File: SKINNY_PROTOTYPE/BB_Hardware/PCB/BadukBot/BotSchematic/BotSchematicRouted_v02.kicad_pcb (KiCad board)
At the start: 4 copper layers, 93 x 44.5 mm, 82 parts, among them J1 MOLEX_78171-0002, J10 A3-16DA-2SV(71), J11 62401621722, J12 A3-16DA-2SV(71), J13 0877601616, J2 MOLEX_78171-0003, M1 Pos-1a, M2 Neg-1a, M3 Pos-2a, M4 Neg-2a, P1 SWD Pads, P4 Conn_01x02_Female, P5 Pads, Q1 MMBT3904LT1G, Q2 MMBT3904LT1G, Q3 MMBT3904LT1G, Q4 MMBT3904LT1G, U1 STM32F051C8U6, U2 LSM6DS3, U3 A3901SEJTR-T, U4 ADP122ACPZ-3.3-R7, U5 AT42QT1070-MMHCT-ND, U6 MCP73831T-2ACI_OT, U7 NRF24L01P-R7, Y1 7V-16.000MAAE-T

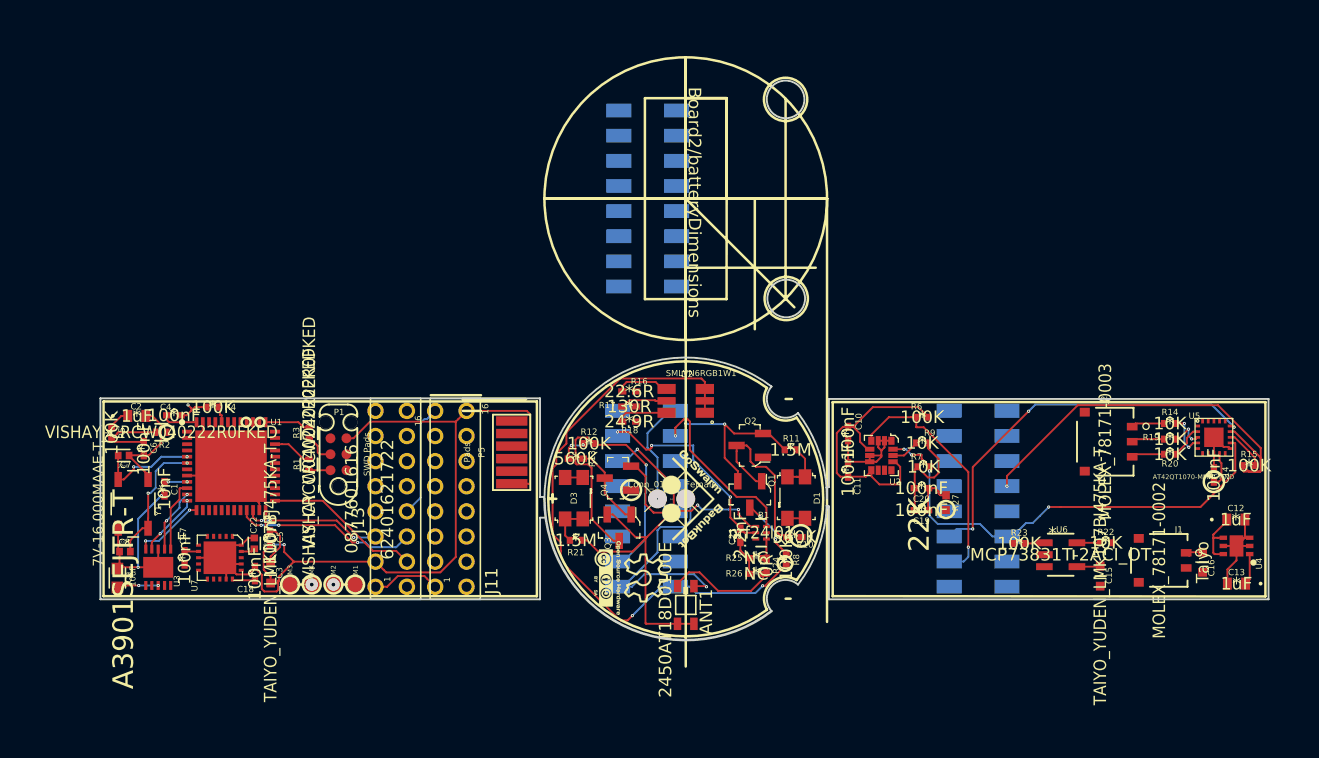
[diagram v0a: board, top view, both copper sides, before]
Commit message: Routed PCBs pending optimization
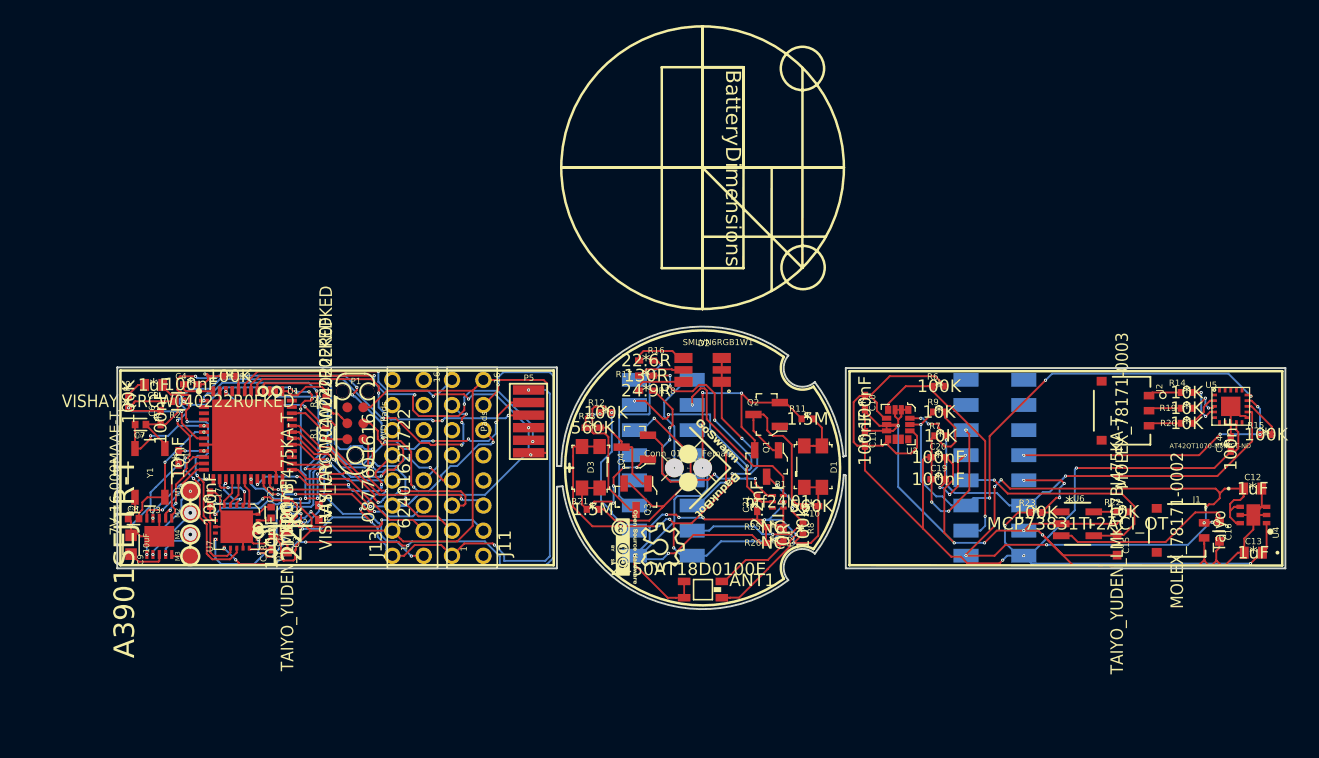
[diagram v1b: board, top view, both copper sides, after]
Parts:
- removed the J12 at (112.5, 86.3)
- J10, J12: footprint A13:A13 -> A13:A13_1
- moved R27 49.9 mm to (85.7, 111.3)
- moved M1 15.1 mm to (75.5, 109.6), turned to 180 degrees
- moved M2 12.7 mm to (75.5, 111.3), turned to 180 degrees
- moved M4 10.5 mm to (75.5, 113.1), turned to 180 degrees
- moved M3 8.26 mm to (75.5, 114.8), turned to 180 degrees
- moved C17 5.10 mm to (77.1, 110.2), turned to 270 degrees
- moved C9 2.86 mm to (70.8, 113.9)
- moved C12 2.81 mm to (160.1, 109.4)
- moved C13 2.81 mm to (160.1, 114.5)
- moved C15 2.81 mm to (149.3, 113.9)
- moved C16 2.81 mm to (157.4, 112.8)
- moved C2 2.81 mm to (72.6, 101.2)
- moved C21 2.81 mm to (120.6, 110.7)
- moved C22 2.81 mm to (81.9, 111.3)
- moved C5 2.81 mm to (83.2, 110.9)
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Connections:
- ANT1 pad 2: 2a_GND -> 23a_Ground
- ANT1 pad 3: 2a_GND -> 23a_Ground
- ANT1 pad 4: 2a_GND -> 23a_Ground
- B1 pad 2: 2a_GND -> 23a_Ground
- C1 pad 2: 2b_GND -> 23a_Ground
- C10 pad 2: 21a_3.3v -> 23a_Ground
- C11 pad 2: 21a_3.3v -> 23a_Ground
- C12 pad 2: 21a_3.3v -> 23a_Ground
- C13 pad 2: 21a_3.3v -> 23a_Ground
- C14 pad 2: 21a_3.3v -> 23a_Ground
- C15 pad 2: 21a_3.3v -> 23a_Ground
- C16 pad 2: 21a_3.3v -> 23a_Ground
- C17 pad 1: 2b_GND -> 23a_Ground
- C18 pad 1: 2b_GND -> 23a_Ground
- C19 pad 1: 2b_GND -> 23a_Ground
- C19 pad 2: 1b_3.3v -> 21a_3.3v
- C2 pad 2: 2b_GND -> 23a_Ground
- C20 pad 1: 2b_GND -> 23a_Ground
- C20 pad 2: 1b_3.3v -> 21a_3.3v
- C21 pad 2: 2a_GND -> 23a_Ground
- C22 pad 2: 2b_GND -> 23a_Ground
- C3 pad 2: 2b_GND -> 23a_Ground
- C4 pad 2: 2b_GND -> 23a_Ground
- C5 pad 2: 2b_GND -> 23a_Ground
- C6 pad 2: 2b_GND -> 23a_Ground
- C7 pad 2: 2b_GND -> 23a_Ground
- C8 pad 2: 2b_GND -> 23a_Ground
- C9 pad 2: 2b_GND -> 23a_Ground
- J1 pad 2: 21a_3.3v -> 23a_Ground
- J10 pad 2: 2a_GND -> 23a_Ground
- J11 pad 16: 2b_GND -> 23a_Ground
- J12 pad 2: 21a_3.3v -> 22a_VBAT
- J12 pad 3: 22a_VBAT -> 23a_Ground
- J13 pad 3: 2b_GND -> 23a_Ground
- P1 pad 5: 2b_GND -> 23a_Ground
- P4 pad 2: 2a_GND -> 23a_Ground
- P5 pad 6: 2b_GND -> 23a_Ground
- Q1 pad 2: 2a_GND -> 23a_Ground
- Q2 pad 2: 2a_GND -> 23a_Ground
- Q3 pad 2: 2a_GND -> 23a_Ground
- Q4 pad 2: 2a_GND -> 23a_Ground
- R11 pad 2: 2a_GND -> 23a_Ground
- R16 pad 1: Net-(R16-Pad1) -> 6a_RGBLED2
- R17 pad 1: Net-(R17-Pad1) -> 5a_RGBLED1
- R18 pad 1: Net-(R18-Pad1) -> 7a_RGBLED3
- R21 pad 1: 2a_GND -> 23a_Ground
- R22 pad 1: 21a_3.3v -> 23a_Ground
- R25 pad 2: 2a_GND -> 23a_Ground
- R26 pad 2: 2a_GND -> 23a_Ground
- R27 pad 1: 2b_GND -> 23a_Ground
- R4 pad 2: 2b_GND -> 23a_Ground
- U1 pad 23: 2b_GND -> 23a_Ground
- U1 pad 47: 2b_GND -> 23a_Ground
- U1 pad 49: 2b_GND -> 23a_Ground
- U1 pad 7: NSRT -> NRST
- U1 pad 8: 2b_GND -> 23a_Ground
- U2 pad 1: 21a_3.3v -> 23a_Ground
- U2 pad 2: 21a_3.3v -> 23a_Ground
- U2 pad 3: 21a_3.3v -> 23a_Ground
- U2 pad 6: 21a_3.3v -> 23a_Ground
- U2 pad 7: 21a_3.3v -> 23a_Ground
- U2 pad 9: 21a_3.3v -> Net-(U2-Pad9)
- U3 pad 11: 2b_GND -> 23a_Ground
- U3 pad 3: 2b_GND -> 23a_Ground
- U4 pad 2: 21a_3.3v -> 23a_Ground
- U4 pad 3: 21a_3.3v -> 23a_Ground
- U4 pad 5: 21a_3.3v -> 23a_Ground
- U4 pad 7: 21a_3.3v -> 23a_Ground
- U5 pad 11: 21a_3.3v -> 23a_Ground
- U5 pad 13: 21a_3.3v -> 23a_Ground
- U5 pad 44: 21a_3.3v -> 23a_Ground
- U5 pad 8: 21a_3.3v -> 23a_Ground
- U5 pad 9: 21a_3.3v -> 23a_Ground
- U6 pad 2: 21a_3.3v -> 23a_Ground
- U7 pad 14: 2b_GND -> 23a_Ground
- U7 pad 17: 2b_GND -> 23a_Ground
- U7 pad 20: 2b_GND -> 23a_Ground
- U7 pad 21: 2b_GND -> 23a_Ground
- U7 pad 8: 2b_GND -> 23a_Ground
- Y1 pad 2: 2b_GND -> 23a_Ground
- Y1 pad 4: 2b_GND -> 23a_Ground
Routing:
- net 23a_Ground: track 0.00 -> 212.1 mm, vias 0 -> 17
- net 2b_GND: track 111.4 -> 0.00 mm, vias 5 -> 0
- net 2a_GND: track 2.87 -> 98.3 mm, vias 1 -> 12
- net 15a_GND2: track 70.6 -> 0.00 mm, vias 4 -> 0
- net 21a_3.3v: track 53.6 -> 121.3 mm, vias 0 -> 8
- net 22a_VBAT: track 6.42 -> 72.4 mm, vias 0 -> 7
- net 12b_ANT1: track 0.00 -> 55.7 mm, vias 0 -> 8
- net 14b_VDD_PA: track 0.00 -> 51.1 mm, vias 0 -> 6
- net 13b_ANT2: track 0.00 -> 48.1 mm, vias 0 -> 7
- net 10b_SDA: track 11.0 -> 53.7 mm, vias 3 -> 7
- net 1b_3.3v: track 31.8 -> 74.4 mm, vias 4 -> 11
- net Net-(P1-Pad3): track 0.00 -> 36.1 mm, vias 0 -> 10
- net 22b_VBAT: track 0.00 -> 30.7 mm, vias 0 -> 6
- net 8b_IO1: track 0.00 -> 30.7 mm, vias 0 -> 4
- net 11b_SCL: track 14.7 -> 44.4 mm, vias 3 -> 7
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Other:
- board size 93 x 44.5 mm -> 93 x 22.5 mm
- board text added: "BatteryDimensions"
- board text added: "j13-10"
- board text added: "j13-12"
- board text removed: "Board2/batteryDimensions"

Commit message: Updates to the BOM; PCB changes
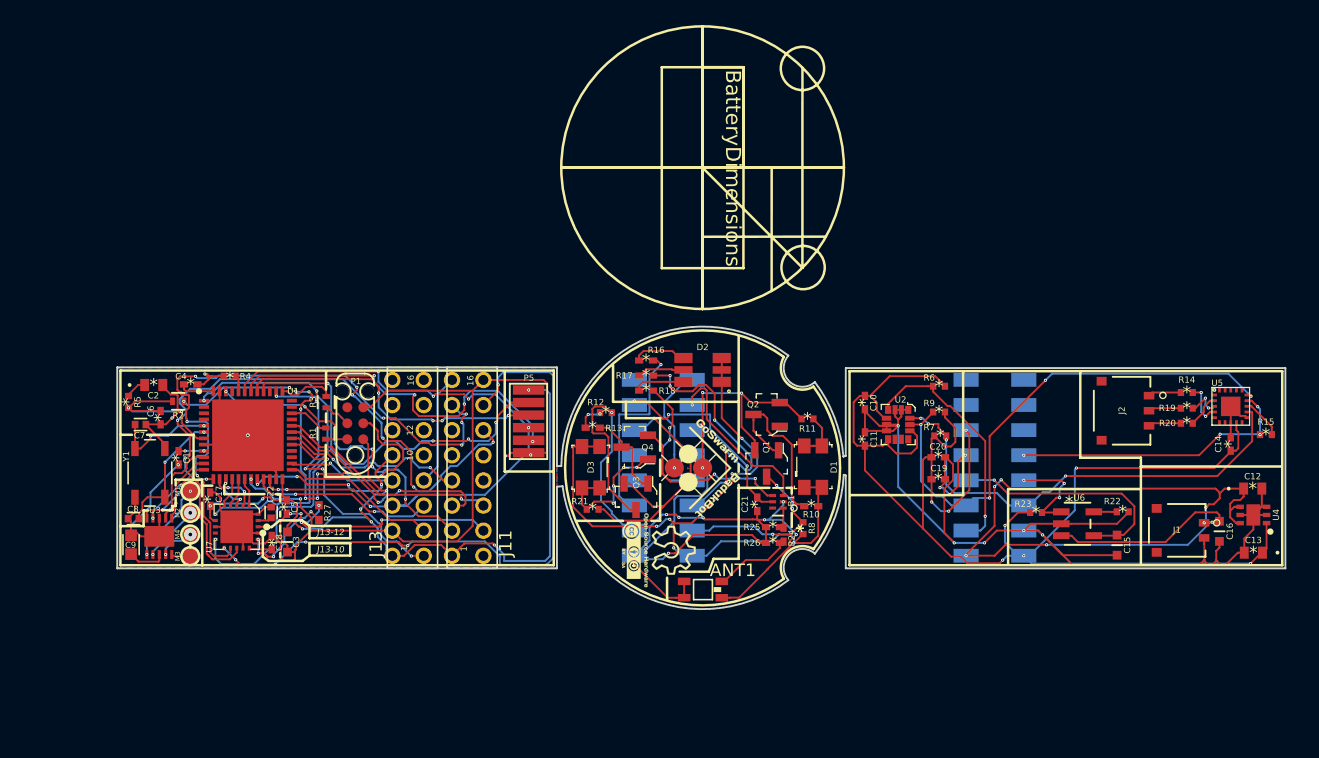
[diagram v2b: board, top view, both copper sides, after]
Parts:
- moved G2 0.91 mm to (112.8, 114.3)
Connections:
- ANT1 pad 2: 23a_Ground -> 2a_GND
- ANT1 pad 3: 23a_Ground -> 2a_GND
- ANT1 pad 4: 23a_Ground -> 2a_GND
- B1 pad 2: 23a_Ground -> 2a_GND
- C1 pad 2: 23a_Ground -> 2b_GND
- C17 pad 1: 23a_Ground -> 2b_GND
- C18 pad 1: 23a_Ground -> 2b_GND
- C2 pad 2: 23a_Ground -> 2b_GND
- C21 pad 2: 23a_Ground -> 2a_GND
- C22 pad 2: 23a_Ground -> 2b_GND
- C3 pad 2: 23a_Ground -> 2b_GND
- C4 pad 2: 23a_Ground -> 2b_GND
- C5 pad 2: 23a_Ground -> 2b_GND
- C6 pad 2: 23a_Ground -> 2b_GND
- C7 pad 2: 23a_Ground -> 2b_GND
- C8 pad 2: 23a_Ground -> 2b_GND
- C9 pad 2: 23a_Ground -> 2b_GND
- J10 pad 2: 23a_Ground -> 2a_GND
- J11 pad 16: 23a_Ground -> 2b_GND
- J13 pad 3: 23a_Ground -> 2b_GND
- P1 pad 5: 23a_Ground -> 2b_GND
- P4 pad 2: 23a_Ground -> 2a_GND
- P5 pad 6: 23a_Ground -> 2b_GND
- Q1 pad 2: 23a_Ground -> 2a_GND
- Q2 pad 2: 23a_Ground -> 2a_GND
- Q3 pad 2: 23a_Ground -> 2a_GND
- Q4 pad 2: 23a_Ground -> 2a_GND
- R11 pad 2: 23a_Ground -> 2a_GND
- R21 pad 1: 23a_Ground -> 2a_GND
- R25 pad 2: 23a_Ground -> 2a_GND
- R26 pad 2: 23a_Ground -> 2a_GND
- R27 pad 1: 23a_Ground -> 2b_GND
- R4 pad 2: 23a_Ground -> 2b_GND
- U1 pad 23: 23a_Ground -> 2b_GND
- U1 pad 47: 23a_Ground -> 2b_GND
- U1 pad 49: 23a_Ground -> 2b_GND
- U1 pad 8: 23a_Ground -> 2b_GND
- U3 pad 11: 23a_Ground -> 2b_GND
- U3 pad 3: 23a_Ground -> 2b_GND
- U7 pad 14: 23a_Ground -> 2b_GND
- U7 pad 17: 23a_Ground -> 2b_GND
- U7 pad 20: 23a_Ground -> 2b_GND
- U7 pad 21: 23a_Ground -> 2b_GND
- U7 pad 8: 23a_Ground -> 2b_GND
- Y1 pad 2: 23a_Ground -> 2b_GND
- Y1 pad 4: 23a_Ground -> 2b_GND
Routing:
- net 2b_GND: track 0.00 -> 118.8 mm, vias 0 -> 13
- net 23a_Ground: track 212.1 -> 98.4 mm, vias 17 -> 8
- added copper zone on F.Cu, net 1b_3.3v
- added copper zone on B.Cu, net 2b_GND
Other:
- copper layers 4 -> 2
- board text added: "10"
- board text added: "12"
- board text added: "J13-10"
- board text added: "J13-12"
- board text removed: "j13-10"
- board text removed: "j13-12"

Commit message: Updated copper cores; changed schematic naming flags for 3rd party BOM generator; added renders of board; added some datasheets
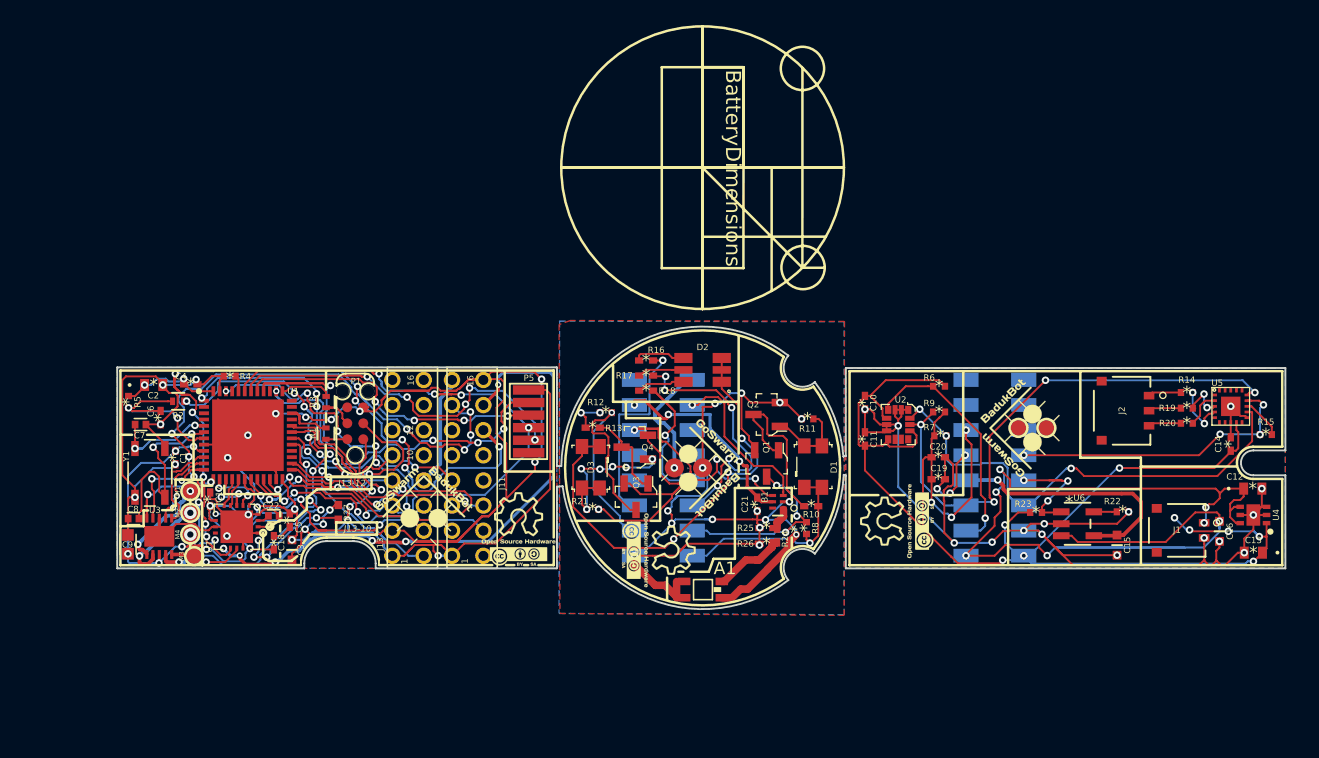
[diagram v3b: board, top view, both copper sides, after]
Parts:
- removed ANT1: 2450AT18D0100E, 2450AT18D0100E:DFN320X160X120-4RN
- added A1: 2450AT18D0100E, 2450AT18D0100E:DFN320X160X120-4RN, F.Cu at (116.3, 117.5)
- added G1: LOGO, Silk:BadukBot-GoSwarm, F.Cu at (141.7, 104.6)
- added G1: LOGO, Silk:BadukBot-GoSwarm, F.Cu at (94.1, 110.9)
- added G2: LOGO, Silk:OpenHardwareLogo, F.Cu at (101.6, 112.6)
- added G2: LOGO, Silk:OpenHardwareLogo, F.Cu at (131.8, 112.0)
- added G5: LOGO, Silk:links_20mm, B.Cu at (80.2, 108.2)
- added G6: LOGO, Silk:links_20mm, B.Cu at (152.7, 109.3)
- added G7: LOGO, Silk:links_20mm, B.Cu at (119.6, 107.7)
- added TESTPOINT-50MIL: VAL**, gsg-modules:TESTPOINT-50MIL, F.Cu at (143.7, 104.6)
- added TESTPOINT-50MIL: VAL**, gsg-modules:TESTPOINT-50MIL, F.Cu at (141.4, 104.6)
- C19: value 100nF -> 10nF
- C20: value 100nF -> 1nF
- J1: value MOLEX_78171-0002 -> MOLEX781710002
- J10, J12: value A3-16DA-2SV(71) -> A316DA2SV71
- J2: value MOLEX_78171-0003 -> MOLEX781710003
- M1: value Pos-1a -> Pos1a
- M2: value Neg-1a -> Neg1a
- M3: value Pos-2a -> Pos2a
- M4: value Neg-2a -> Neg2a
- P1: value SWD Pads -> SWDPads
- P4: value Conn_01x02_Female -> Conn01x02Female
- U3: value A3901SEJTR-T -> A3901SEJTRT
- U4: value ADP122ACPZ-3.3-R7 -> ADP122ACPZ33R7
- U5: value AT42QT1070-MMHCT-ND -> AT42QT1070MMHCTND
- U6: value MCP73831T-2ACI_OT -> MCP73831T2ACIOT
- U7: value NRF24L01P-R7 -> NRF24L01PR7
- Y1: value 7V-16.000MAAE-T -> 7V16000MAAET
- moved R27 1.55 mm to (87.3, 111.3)
- moved C5 1.07 mm to (83.4, 111.9)
- moved C3 0.73 mm to (83.6, 114.3)
- moved R24 0.52 mm to (122.2, 113.1)
- moved R25 0.52 mm to (121.4, 112.5)
- moved R26 0.52 mm to (121.4, 113.8)
- moved C22 0.34 mm to (82.1, 111.6), turned to 0 degrees
- moved M3 0.31 mm to (75.8, 114.8)
- moved R8 0.27 mm to (124.5, 112.5)
- moved C1 0.26 mm to (74.3, 106.9)
- moved C9 0.25 mm to (70.5, 113.8)
- moved C18 0.17 mm to (82.2, 113.7)
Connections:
- net 10b_SDA renamed 10bSDA
- net 11b_SCL renamed 11bSCL
- net 12a_ANT1 renamed 12aA1
- net 12b_ANT1 renamed 12bA1
- net 13a_ANT2 renamed 13aA2
- net 13b_ANT2 renamed 13bA2
- net 14a_VDD_PA renamed 14aVDDPA
- net 14b_VDD_PA renamed 14bVDDPA
- net 15a_P4-1 renamed 15aP41
- net 15b_P4-1 renamed 15bP41
- net 1a_3.3v renamed 1a33v
- net 1b_3.3v renamed 1b33v
- net 22a_VBAT renamed 22aVBAT
- net 22b_VBAT renamed 22bVBAT
- net 24a_IMU_INT renamed 24aIMUINT
- net 24b_IMU_INT renamed 24bIMUINT
- net 25a_SDA renamed 25aSDA
- net 26a_SCL renamed 26aSCL
- net 27a_CHARGING renamed 27aCHARGING
- net 27b_CHARGING renamed 27bCHARGING
- net 28a_P4-1 renamed 28aP41
- net 2a_GND renamed 2aGND
- net 2b_GND renamed 2bGND
- net 3a_PHOTODIODE1 renamed 3aPHOTODIODE1
- net 3b_PHOTODIODE1 renamed 3bPHOTODIODE1
- net 4a_PHOTODIODE2 renamed 4aPHOTODIODE2
- net 4b_PHOTODIODE2 renamed 4bPHOTODIODE2
- net 5a_RGBLED1 renamed 5aRGBLED1
- net 5b_RGBLED1 renamed 5bRGBLED1
- net 6a_RGBLED2 renamed 6aRGBLED2
- net 6b_RGBLED2 renamed 6bRGBLED2
- net 7a_RGBLED3 renamed 7aRGBLED3
- net 7b_RGBLED3 renamed 7bRGBLED3
- net 8b_IO1 renamed 8bIO1
- net 9b_IO2 renamed 9bIO2
- net MCU_X1_16MHZ renamed MCUX116MHZ
- net MCU_X2_16MHZ renamed MCUX216MHZ
- net MOTOR_CONTROL1 renamed MOTORCONTROL1
- net MOTOR_CONTROL2 renamed MOTORCONTROL2
- net MOTOR_CONTROL3 renamed MOTORCONTROL3
- net MOTOR_CONTROL4 renamed MOTORCONTROL4
- net RADIO_IRQ renamed RADIOIRQ
- net ~29a_TOUCH_CHG~ renamed ~29aTOUCHCHG~
- net ~29b_TOUCH_CHG~ renamed ~29bTOUCHCHG~
- C10 pad 1: 21a_3.3v -> 21a33v
- C10 pad 2: 23a_Ground -> 23aGround
- C11 pad 1: 21a_3.3v -> 21a33v
- C11 pad 2: 23a_Ground -> 23aGround
- C12 pad 2: 23a_Ground -> 23aGround
- C13 pad 1: 21a_3.3v -> 21a33v
- C13 pad 2: 23a_Ground -> 23aGround
- C14 pad 1: 21a_3.3v -> 21a33v
- C14 pad 2: 23a_Ground -> 23aGround
- C15 pad 2: 23a_Ground -> 23aGround
- C16 pad 2: 23a_Ground -> 23aGround
- C19 pad 1: 23a_Ground -> 23aGround
- C19 pad 2: 21a_3.3v -> 21a33v
- C20 pad 2: 21a_3.3v -> 21a33v
- J1 pad 2: 23a_Ground -> 23aGround
- J12 pad 1: 21a_3.3v -> 21a33v
- J12 pad 3: 23a_Ground -> 23aGround
- R15 pad 2: 21a_3.3v -> 21a33v
- R22 pad 1: 23a_Ground -> 23aGround
- R23 pad 1: 21a_3.3v -> 21a33v
- R6 pad 2: 21a_3.3v -> 21a33v
- R7 pad 2: 21a_3.3v -> 21a3.3v
- R9 pad 2: 21a_3.3v -> 21a3.3v
- U1 pad 29: RADIO_CLK -> RADIOCLK
- U2 pad 1: 23a_Ground -> 23aGround
- U2 pad 12: 21a_3.3v -> 21a33v
- U2 pad 2: 23a_Ground -> 23aGround
- U2 pad 3: 23a_Ground -> 23aGround
- U2 pad 5: 21a_3.3v -> 21a33v
- U2 pad 6: 23a_Ground -> 23aGround
- U2 pad 7: 23a_Ground -> 23aGround
- U2 pad 8: 21a_3.3v -> 21a33v
- U4 pad 1: 21a_3.3v -> 21a33v
- U4 pad 2: 23a_Ground -> 23aGround
- U4 pad 3: 23a_Ground -> 23aGround
- U4 pad 5: 23a_Ground -> 23aGround
- U4 pad 7: 23a_Ground -> 23aGround
- U5 pad 11: 23a_Ground -> 23aGround
- U5 pad 13: 23a_Ground -> 23aGround
- U5 pad 44: 23a_Ground -> 23aGround
- U5 pad 8: 23a_Ground -> 23aGround
- U5 pad 9: 23a_Ground -> 23aGround
- U6 pad 2: 23a_Ground -> 23aGround
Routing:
- net 2aGND: track 98.4 -> 0.00 mm, vias 12 -> 17
- net 2a_GND: track 0.00 -> 97.5 mm
- net 2bGND: track 118.8 -> 167.9 mm, vias 13 -> 19
- net 1b33v: track 74.4 -> 121.6 mm, vias 11 -> 18
- net 22aVBAT: track 72.4 -> 86.0 mm
- net 7a_RGBLED3: track 0.00 -> 12.4 mm, vias 0 -> 1
- net 7aRGBLED3: track 9.94 -> 0.00 mm, vias 2 -> 0
- net Net-(J12-Pad12): track 0.00 -> 9.86 mm, vias 0 -> 2
- net 12bA1: track 55.7 -> 64.9 mm, vias 8 -> 10
- net ~29bTOUCHCHG~: track 14.6 -> 23.1 mm
- net 23a_Ground: track 98.4 -> 91.6 mm, vias 8 -> 0
- net 8bIO1: track 30.7 -> 37.3 mm
- net Net-(P1-Pad3): track 36.1 -> 29.6 mm, vias 10 -> 8
- net MCUX216MHZ: track 10.3 -> 15.8 mm
- net 13bA2: track 48.1 -> 53.4 mm, vias 7 -> 9
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- added copper zone on B.Cu, net 1a33v
- added copper zone on B.Cu, net 1b33v
- added copper zone on F.Cu, net 21a33v
- added copper zone on B.Cu, net 23a_Ground
- added copper zone on F.Cu, net 2aGND
- added copper zone on F.Cu, net 2bGND
- removed copper zone on F.Cu, net 1b33v
- removed copper zone on B.Cu, net 2bGND
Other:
- outline, holes or cut-outs redrawn
- net class Default: via_dia 0.254 -> 0.6; via_drill 0.1016 -> 0.3
